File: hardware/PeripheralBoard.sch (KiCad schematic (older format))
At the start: 15 parts, among them J1 PARAM1_CV, J2 PARAM2_CV, J3 CLK/TRG, J4 DITTO, J5 OUT1, J6 OUT2, J7 B1_HDR_LEFT, J8 B1_HDR_RIGHT

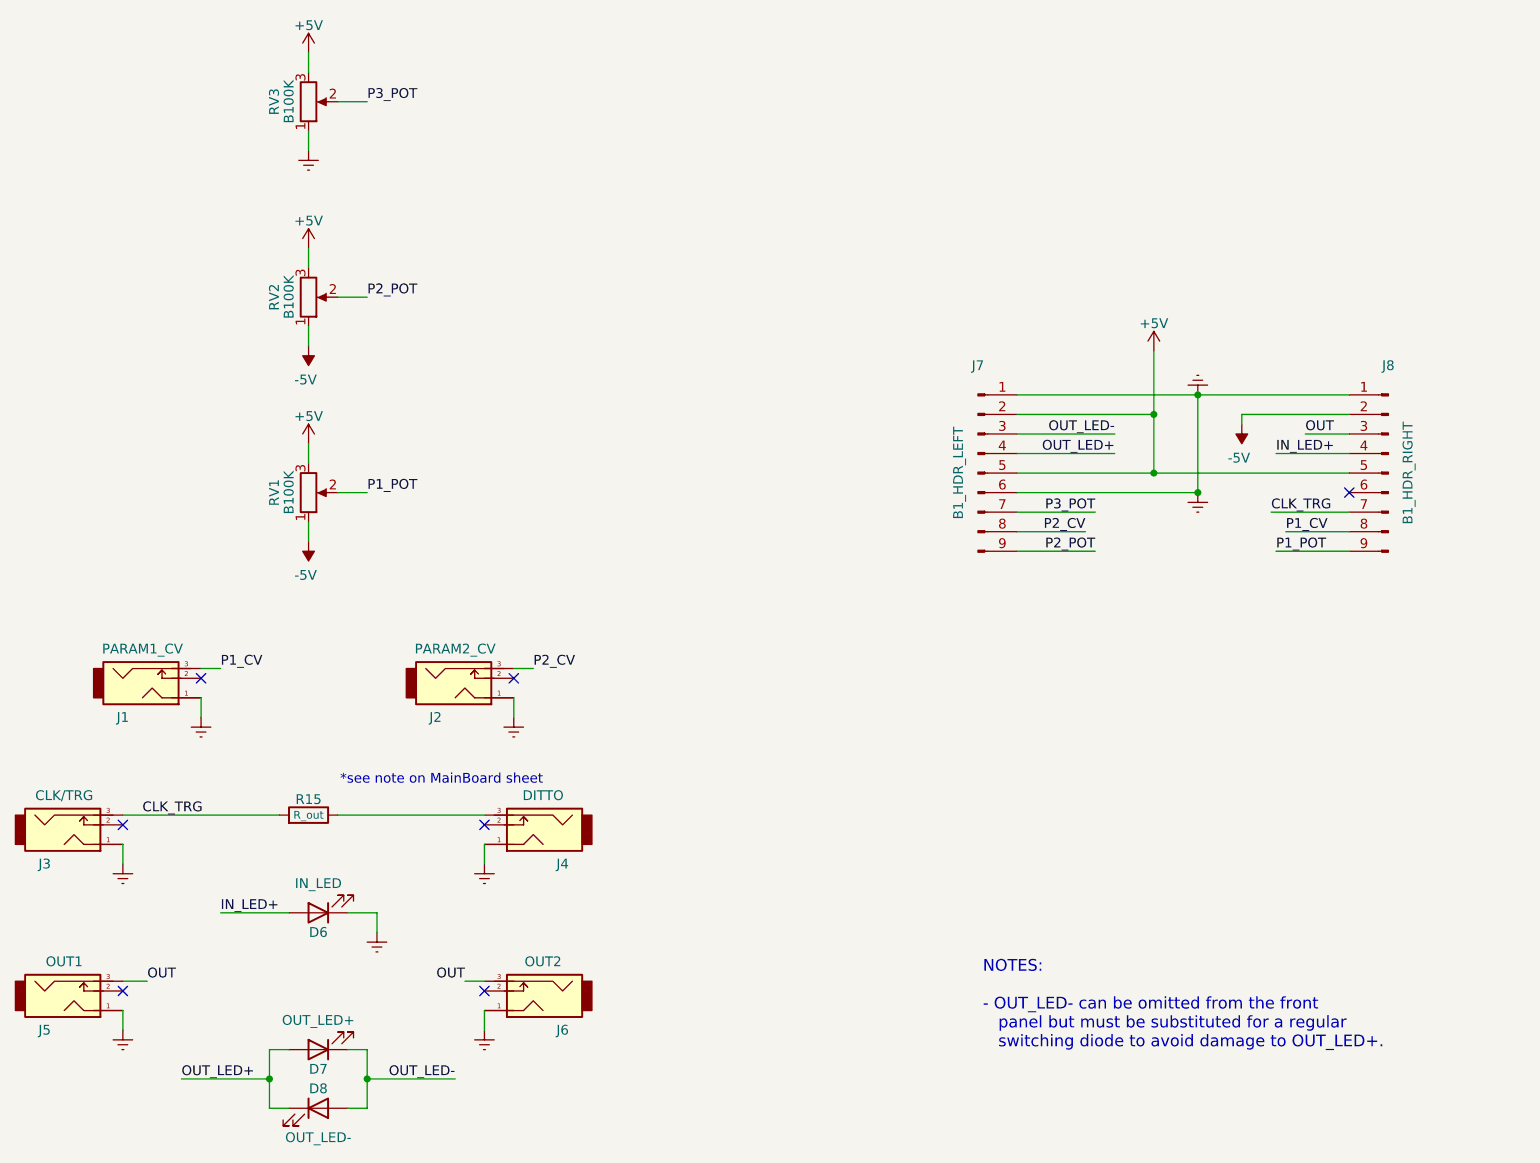
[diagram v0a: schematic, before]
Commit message: [JNTUB-HW] Overhaul PCB layout
- Make traces and clearances much bigger than first attempt
- Remove test points and resistor leading to MCU RESET
- Move some resistors to peripheral board
- Space out remaining components on main board
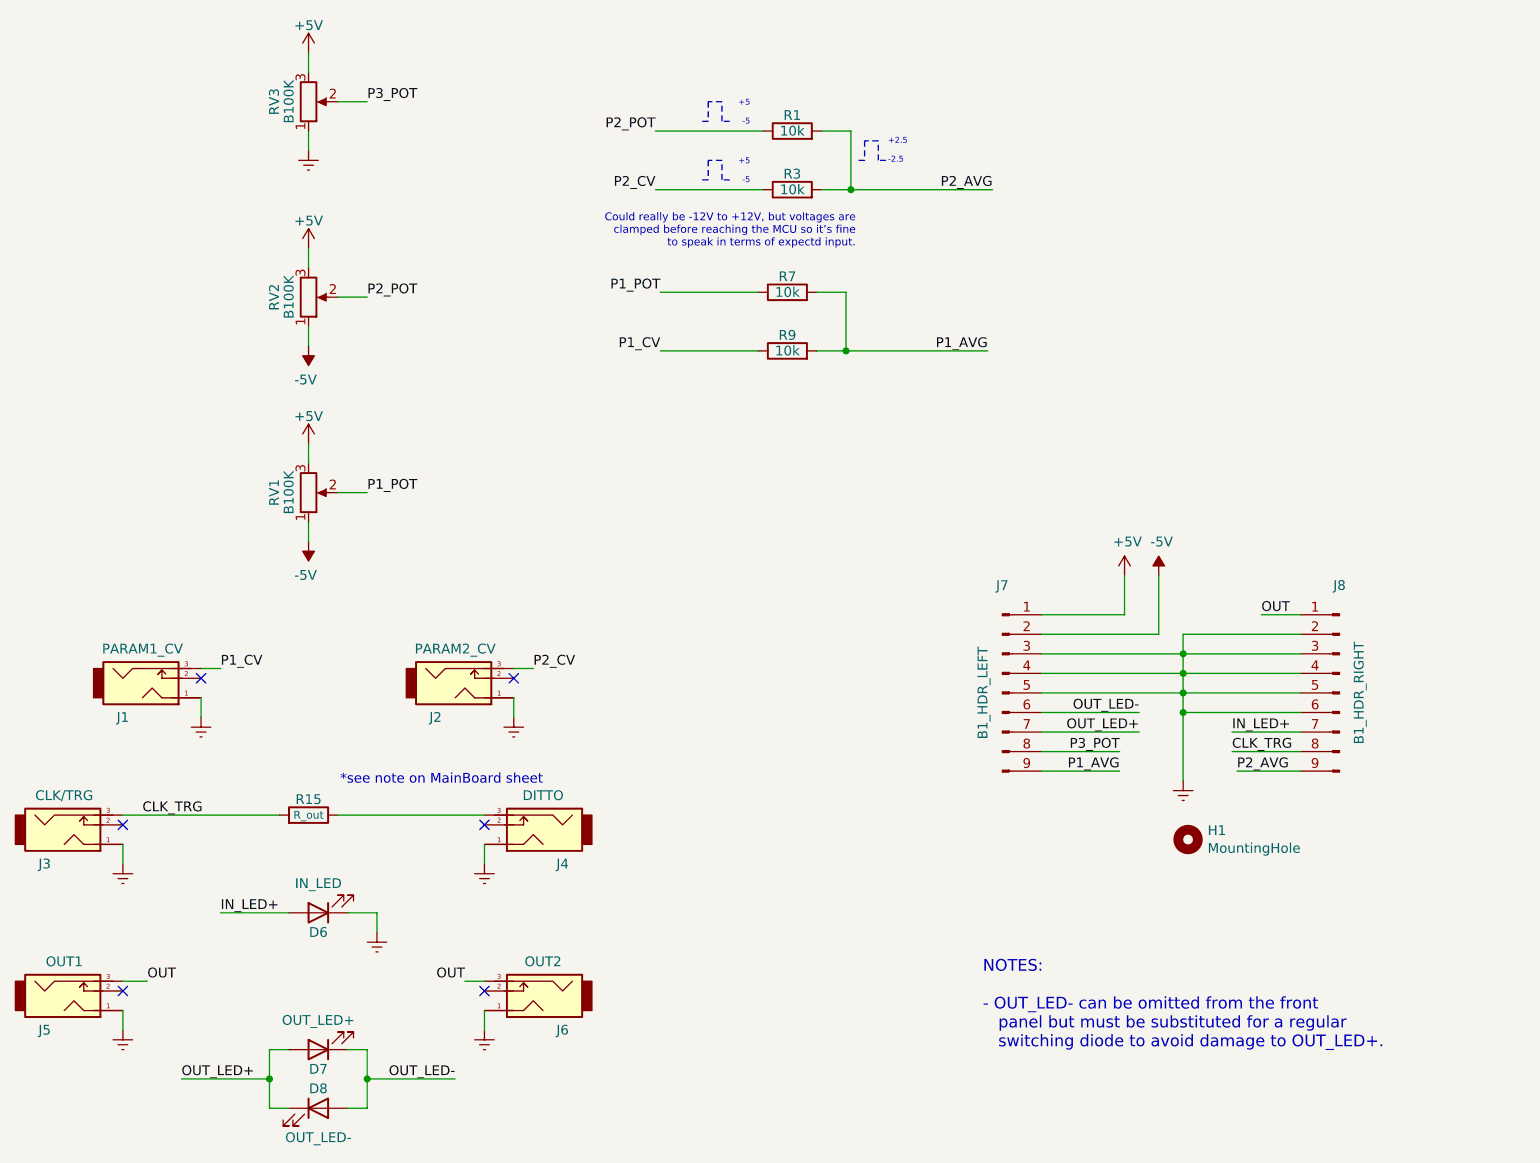
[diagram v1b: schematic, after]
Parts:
- added H1: MountingHole, Mounting_Holes:MountingHole_3.2mm_M3, symbol Mechanical:MountingHole
- added R1, R3, R7, R9: 10k, SDIY:R_Axial_DIN0204_L3.6mm_D1.6mm_P5.08mm_Horizontal, symbol Device:R
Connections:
- net +5V: now also J7.1 (Pin_1); no longer J7.2 (Pin_2), J7.5 (Pin_5), J8.5 (Pin_5)
- net -5V: now also J7.2 (Pin_2); no longer J8.2 (Pin_2)
- net CLK_TRG: now also J8.8 (Pin_8); no longer J8.7 (Pin_7)
- net GNDREF: now also J7.3 (Pin_3), J7.4 (Pin_4), J7.5 (Pin_5), J8.2 (Pin_2), J8.3 (Pin_3), J8.4 (Pin_4), J8.5 (Pin_5), J8.6 (Pin_6); no longer J7.1 (Pin_1), J7.6 (Pin_6), J8.1 (Pin_1)
- net IN_LED+: now also J8.7 (Pin_7); no longer J8.4 (Pin_4)
- net OUT: now also J8.1 (Pin_1); no longer J8.3 (Pin_3)
- net OUT_LED+: now also J7.7 (Pin_7); no longer J7.4 (Pin_4)
- net OUT_LED-: now also J7.6 (Pin_6); no longer J7.3 (Pin_3)
- net P1_CV: now also R9.1; no longer J8.8 (Pin_8)
- net P1_POT: now also R7.1; no longer J8.9 (Pin_9)
- net P2_CV: now also R3.1; no longer J7.8 (Pin_8)
- net P2_POT: now also R1.1; no longer J7.9 (Pin_9)
- net P3_POT: now also J7.8 (Pin_8); no longer J7.7 (Pin_7)
- new net P1_AVG: J7.9 (Pin_9), R7.2, R9.2
- new net P2_AVG: J8.9 (Pin_9), R1.2, R3.2
- no-connect marks 7 -> 6
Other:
- note added: "+2.5\n\n-2.5"
- note added: "+5\n\n-5"
- note added: "Could really be -12V to +12V, but voltages are\nclamped before reaching the MCU so it’s fine\nto speak in terms of expectd input."
- moved on the sheet: J7, J8
